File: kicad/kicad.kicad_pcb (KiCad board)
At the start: 2 copper layers, 458 x 144 mm, 256 parts, among them J1 USB_B_Micro, J2 SWD, J3 pwr_led+, J4 pwr_led-, J5 caps_led+, J6 caps_led-, U1 AMS1117-3.3, Y1 16MGz, sw1 Esc, sw10 Z, sw100 N5, sw101 N6, sw102 N2, sw103 N1, sw104 N0, sw105 MPlay, sw106 MFwd, sw107 NSlash, sw108 NStar, sw109 N8, sw11 LCtrl, sw110 N9, sw111 NMinus, sw112 NPlus, sw113 NEnter, sw114 N3, sw115 NPeriod, sw12 LSys, sw13 F2, sw14 F3, sw15 2, sw16 3, sw17 W, sw18 E, sw19 S, sw2 F1, sw20 D, sw21 X, sw22 C, sw23 LAlt, sw24 THome, sw25 F4, sw26 F5, sw27 4, sw28 5, sw29 R, sw3 Tilda, sw30 T, sw31 F, sw32 G, sw33 V, sw34 B, sw35 LSpace, sw36 TLeft, sw37 F6, sw38 F7, sw39 6, sw4 1, sw40 7, sw41 Y, sw42 U, sw43 H, sw44 J, sw45 N, sw46 M, sw47 TUp, sw48 TDown, sw49 F8, sw5 Tab, sw50 F9, sw51 8, sw52 9, sw53 I, sw54 O, sw55 K, sw56 L, sw57 Comma, sw58 Period, sw59 RSpace, sw6 Q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

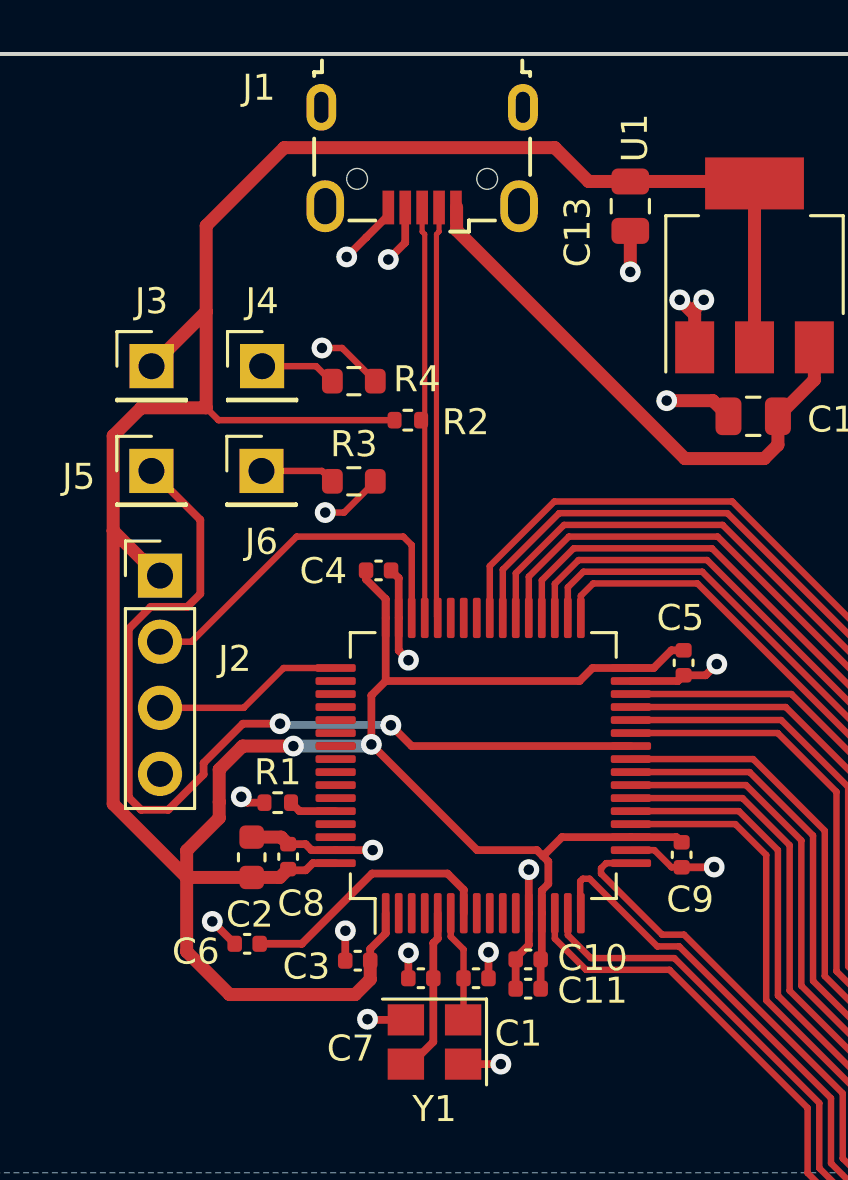
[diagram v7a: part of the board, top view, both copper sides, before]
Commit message: Change thickness of pcb and usb diff pair
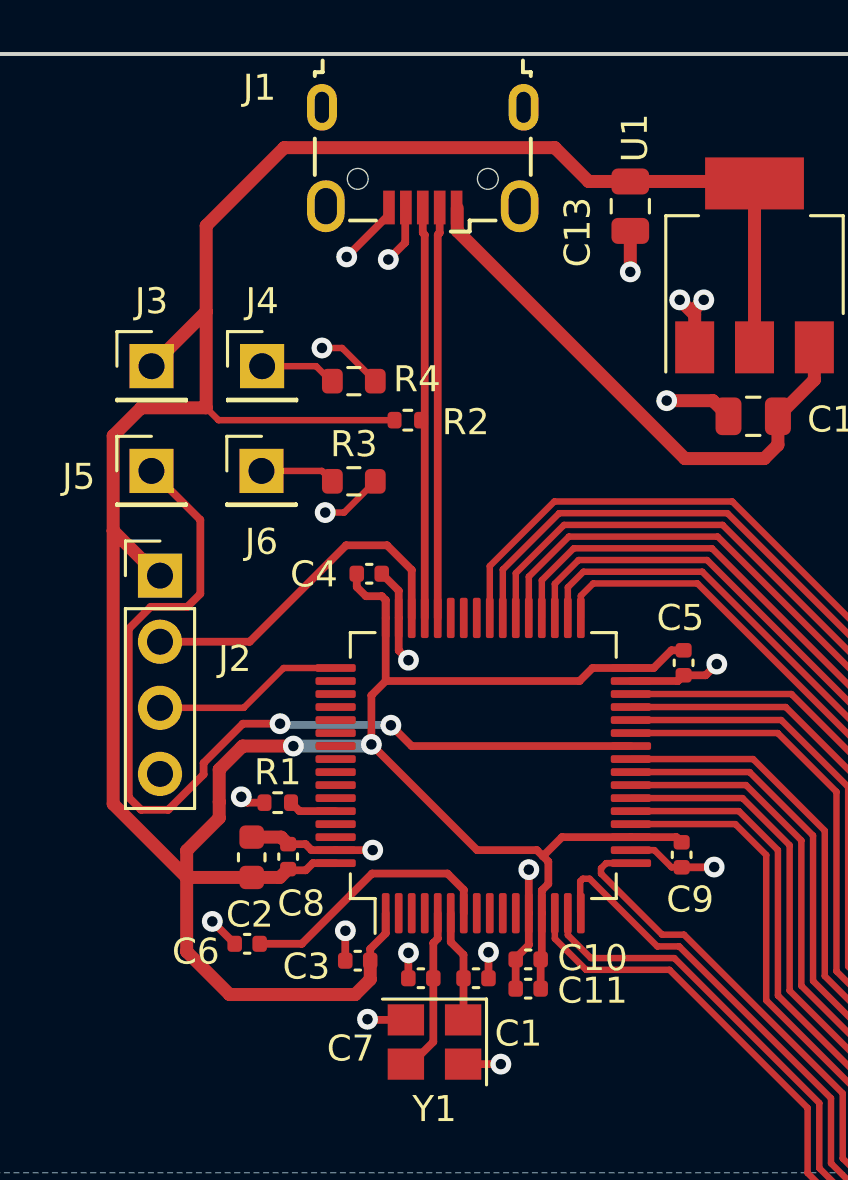
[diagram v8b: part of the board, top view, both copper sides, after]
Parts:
- moved C4 0.38 mm to (69.3, 116.0)
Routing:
- net /SWDIO: track 14.3 -> 13.4 mm
